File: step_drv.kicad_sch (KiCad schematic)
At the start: 64 parts, among them J17 X-STEPPER, J18 Y-STEPPER, J19 ZA-STEPPER, J20 E0-STEPPER, J21 ZB-STEPPER, U6 TMC2226-SA-T, U7 TMC2226-SA-T, U8 TMC2226-SA-T, U9 TMC2226-SA-T

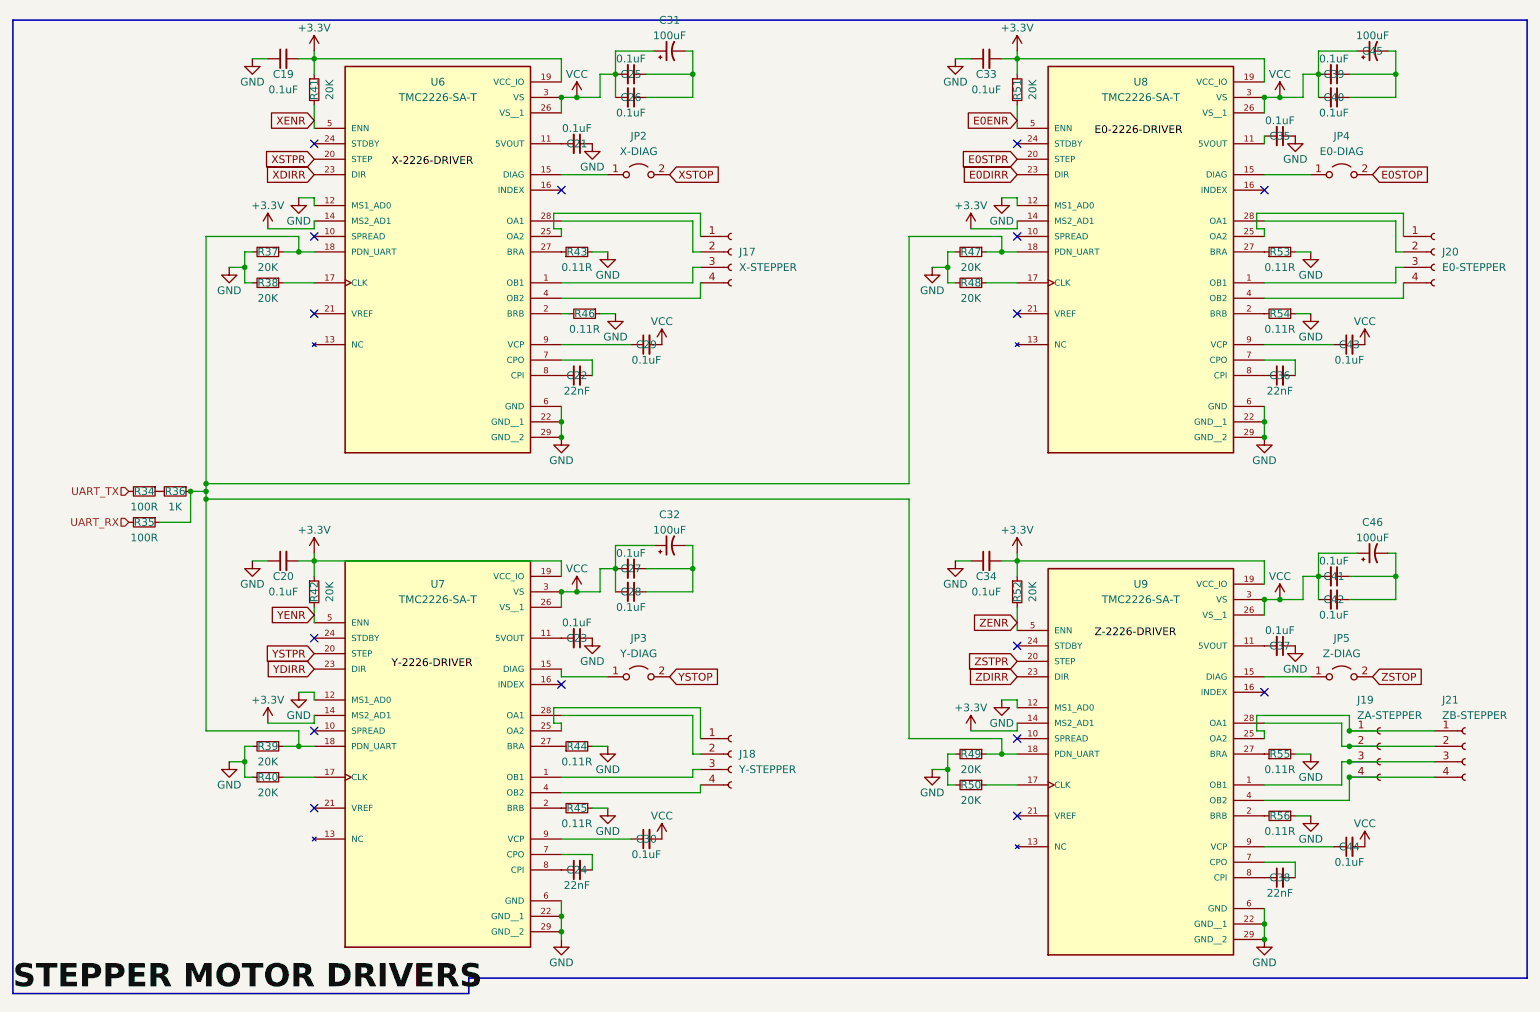
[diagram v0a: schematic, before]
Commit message: Fix driver UART address configuration
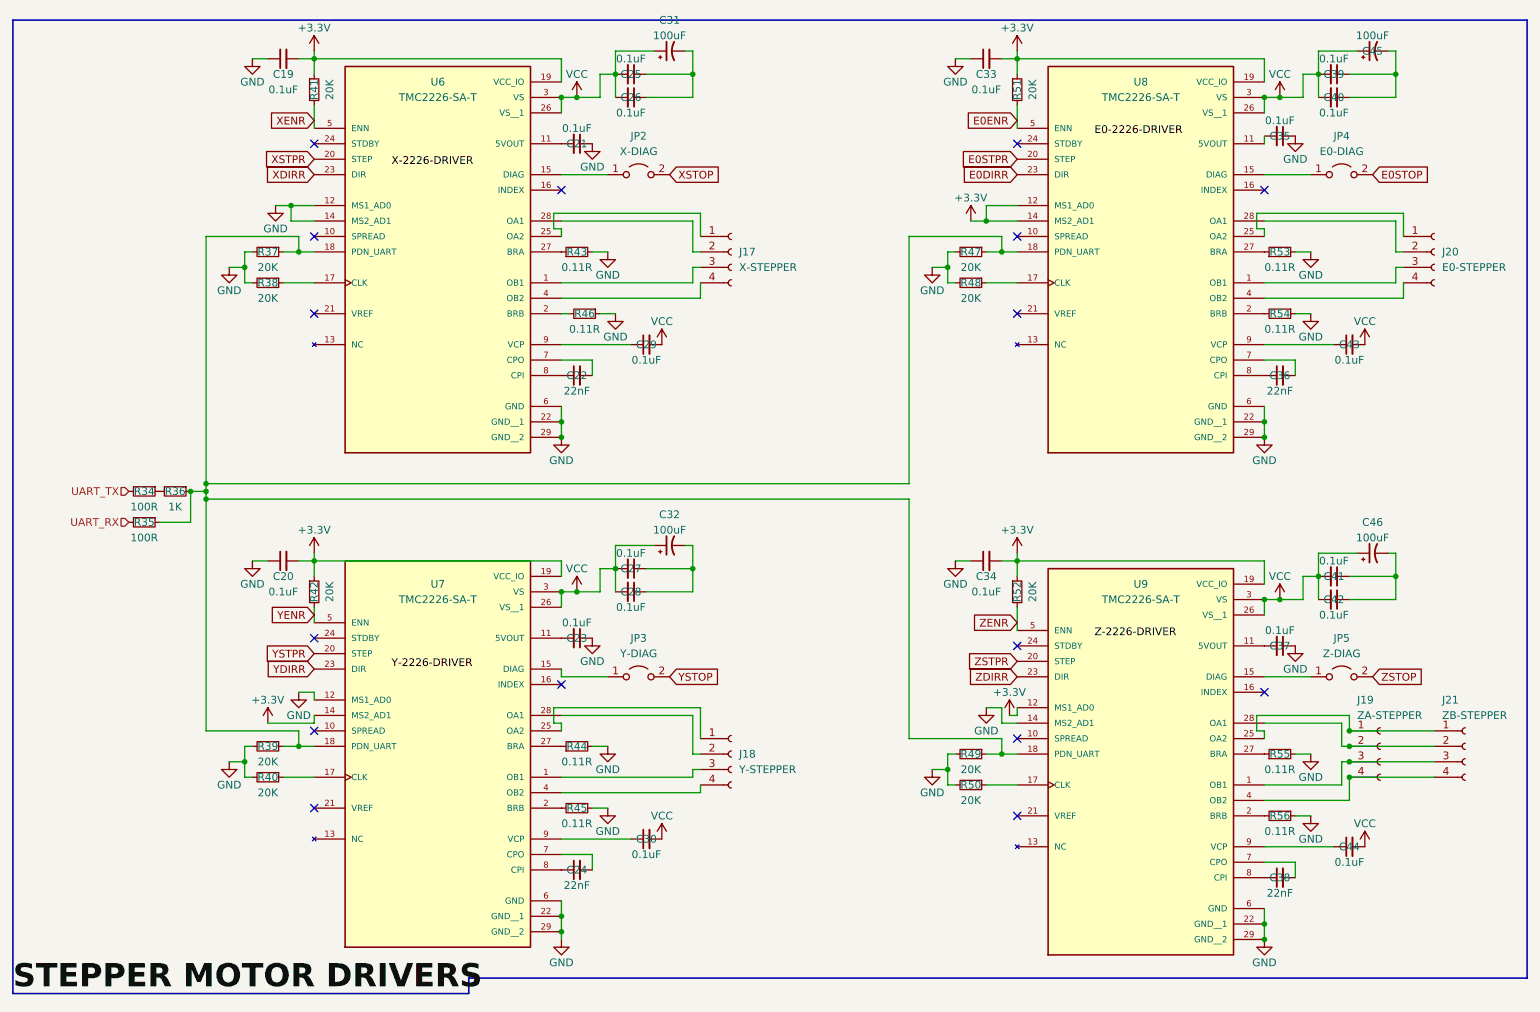
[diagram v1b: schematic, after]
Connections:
- net +3.3V: now also U8.12 (MS1_AD0), U9.12 (MS1_AD0); no longer U6.14 (MS2_AD1), U9.14 (MS2_AD1)
- net GND: now also U6.14 (MS2_AD1), U9.14 (MS2_AD1); no longer U8.12 (MS1_AD0), U9.12 (MS1_AD0)

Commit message: add fan diodes + cleanup + copper fill clearances
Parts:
- C19, C20, C21, C22, C23, C24, C25, C26, C27, C28, C29, C30, C33, C34, C35, C36, C37, C38, C39, C40, C41, C42, C43, C44: footprint Capacitor_SMD:C_0805_2012Metric_Pad1.18x1.45mm_HandSolder -> Capacitor_SMD:C_0805_2012Metric_Pad1.18x1.45mm
- R34, R35, R36, R37, R38, R39, R40, R41, R42, R43, R44, R45, R46, R47, R48, R49, R50, R51, R52, R53, R54, R55, R56: footprint Resistor_SMD:R_0805_2012Metric_Pad1.20x1.40mm_HandSolder -> Resistor_SMD:R_0805_2012Metric_Pad1.20x1.40mm

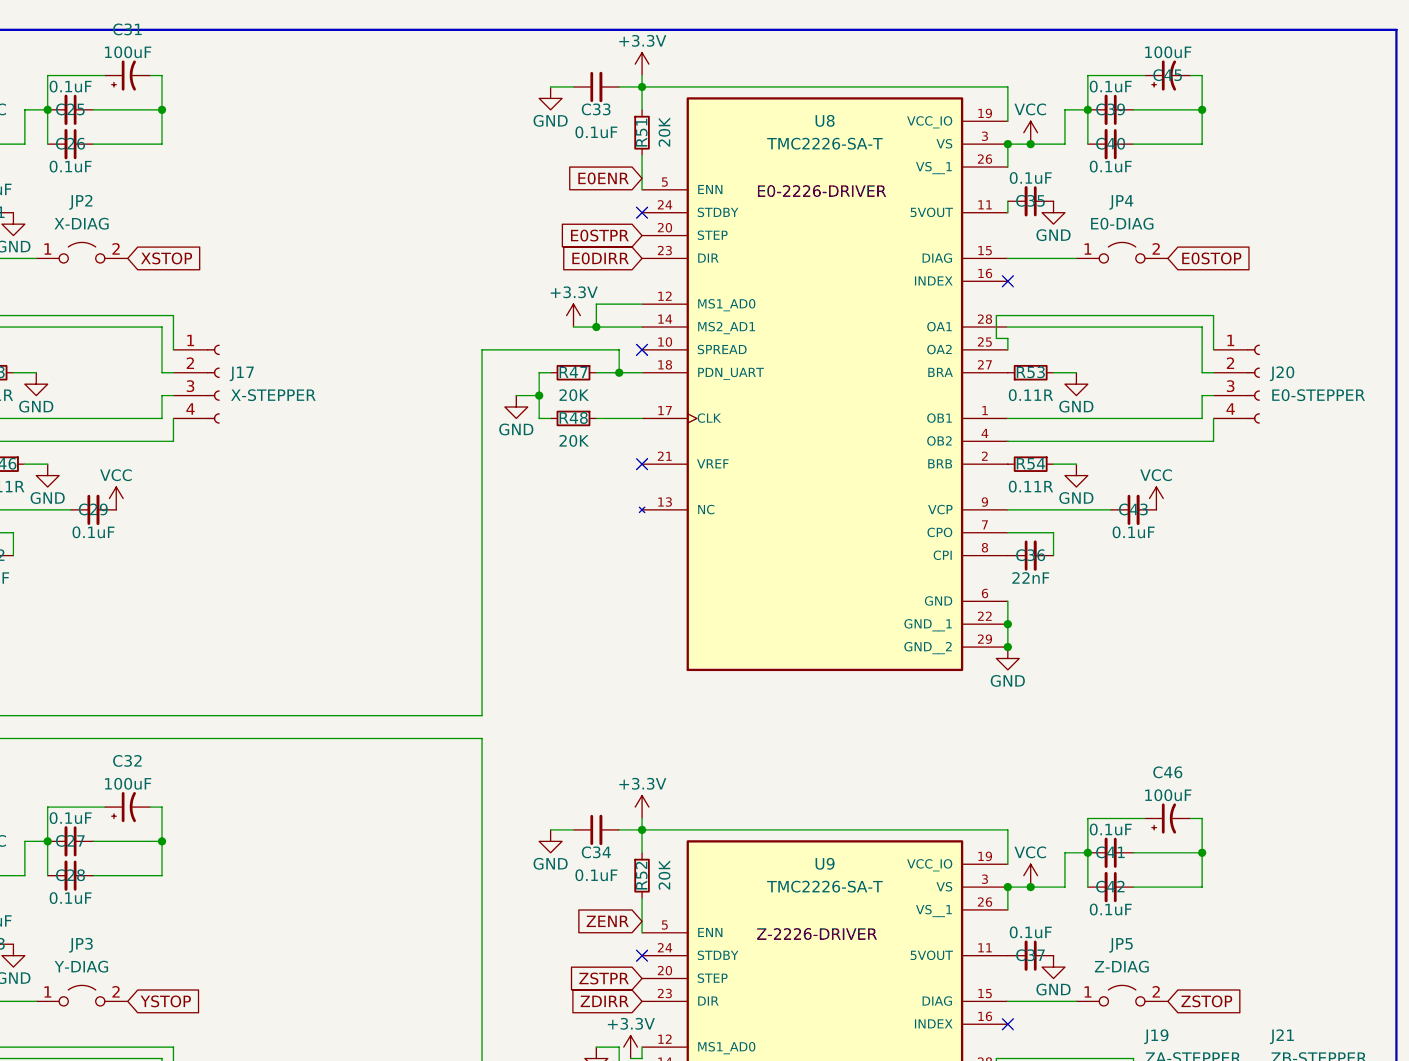
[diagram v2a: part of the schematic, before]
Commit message: Big updates, start of V2, actual RP2040
change from V1.2 to V2 because of many optimizations to come
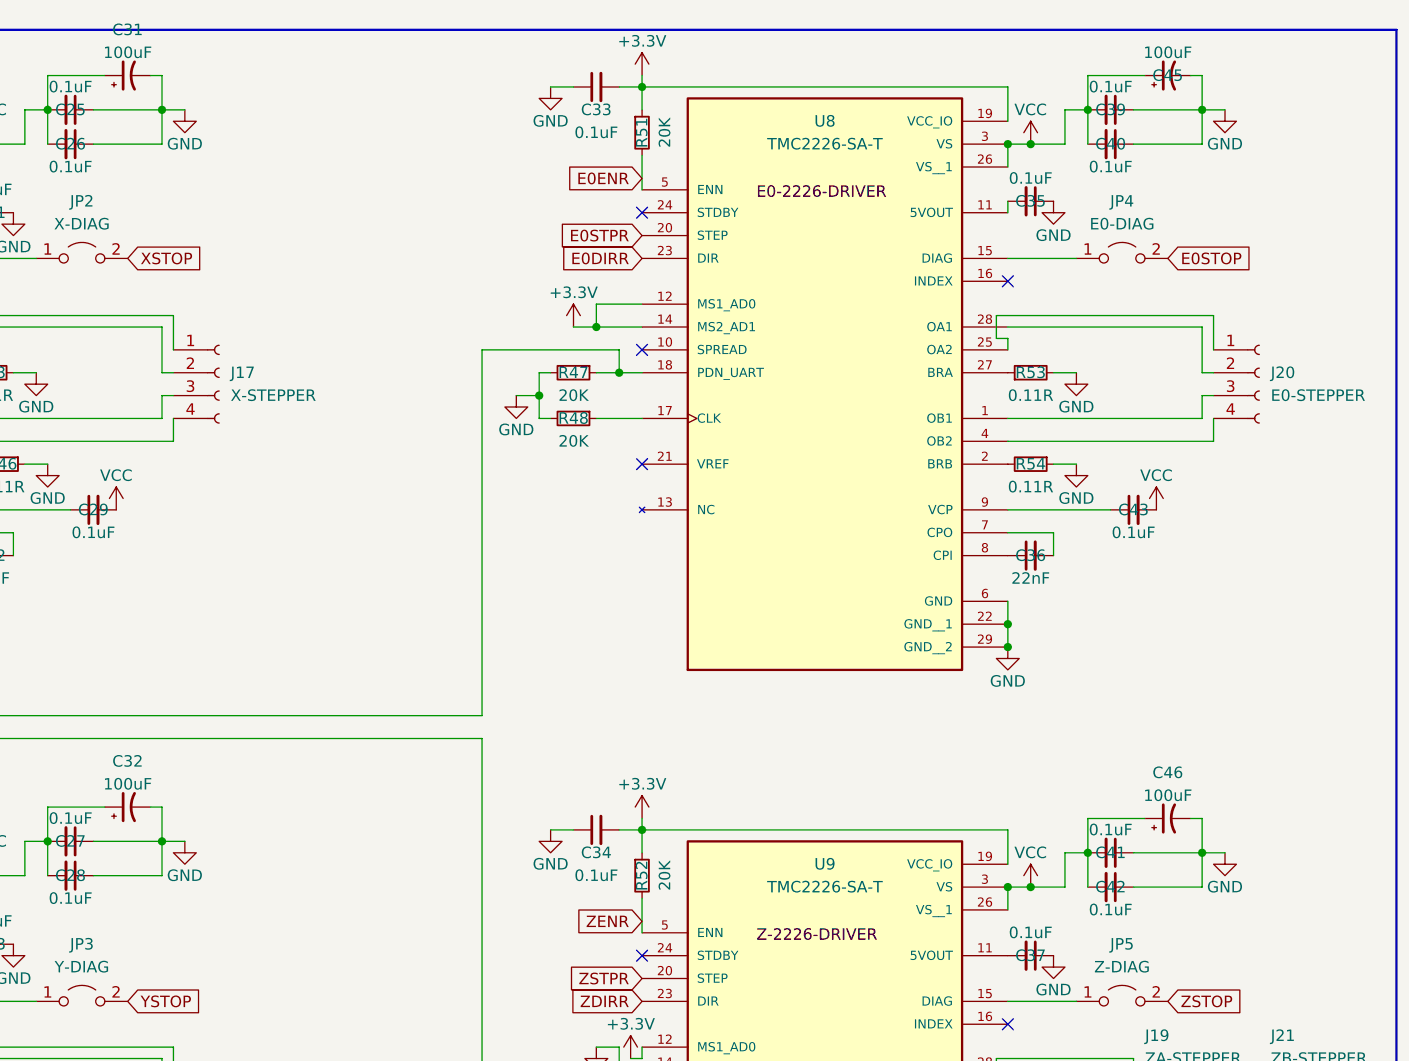
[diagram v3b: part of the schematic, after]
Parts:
- C19, C20, C21, C22, C23, C24, C25, C26, C27, C28, C29, C30, C33, C34, C35, C36, C37, C38, C39, C40, C41, C42, C43, C44: footprint Capacitor_SMD:C_0805_2012Metric_Pad1.18x1.45mm -> Capacitor_SMD:C_0805_2012Metric
- R34, R35, R36, R37, R38, R39, R40, R41, R42, R43, R44, R45, R46, R47, R48, R49, R50, R51, R52, R53, R54, R55, R56: footprint Resistor_SMD:R_0805_2012Metric_Pad1.20x1.40mm -> Resistor_SMD:R_0805_2012Metric
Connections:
- net GND: now also C25.1, C26.1, C27.1, C28.1, C31.2, C32.2, C39.1, C40.1, C41.1, C42.1, C45.2, C46.2

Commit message: Updates, Move to 0602, Optimize Routing
* 0805 -> 0602
* Flash 8MB SOIC8 -> Flash 16MB USON 2x3
* Indev Pic
* Trace Optimization
* Whatever else i forgor
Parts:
- C19, C20, C21, C22, C23, C24, C25, C26, C27, C28, C29, C30, C33, C34, C35, C36, C37, C38, C39, C40, C41, C42, C43, C44: footprint Capacitor_SMD:C_0805_2012Metric -> Capacitor_SMD:C_0603_1608Metric
- R34, R35, R36, R37, R38, R39, R40, R41, R42, R43, R44, R45, R46, R47, R48, R49, R50, R51, R52, R53, R54, R55, R56: footprint Resistor_SMD:R_0805_2012Metric -> Resistor_SMD:R_0603_1608Metric
